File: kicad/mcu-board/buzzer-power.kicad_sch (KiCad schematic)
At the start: 2 parts, among them Q1 Q_NPN_CEB

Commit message: chore?: Saving again, might redo pcb
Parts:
- renumbered R8 to R10
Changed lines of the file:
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@@
 		(dnp no)
 		(fields_autoplaced yes)
-		(property "Reference" "R8"
+		(property "Reference" "R10"
 			(at 99.06 62.23 90)
 			(effects
@@
 			(project ""
 				(path "/f6735569-a094-4d1f-804a-28898efbaebf/56e29116-eeed-430d-b848-aa0aa6b02ec3"
-					(reference "R8")
+					(reference "R10")
 					(unit 1)
 				)

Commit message: chore: Fixed led footprint from 0805 to 0603, and edited title for buzzer
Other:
- company: The Retrievers -> The Retrievers | Designed by aids
- title: (none) -> Buzzer Power
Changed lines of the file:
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@@
 	(paper "A4")
 	(title_block
+		(title "Buzzer Power")
 		(date "2025-12-10")
 		(rev "V1")
-		(company "The Retrievers")
+		(company "The Retrievers | Designed by aids")
 	)
 	(text "Buzzer Power"

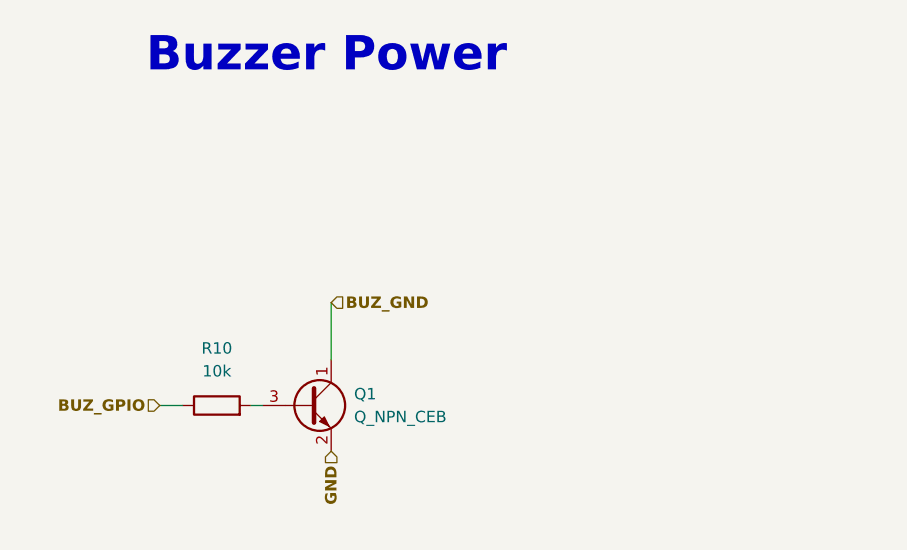
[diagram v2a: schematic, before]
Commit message: feat: finished v2 schematic of mcu-board
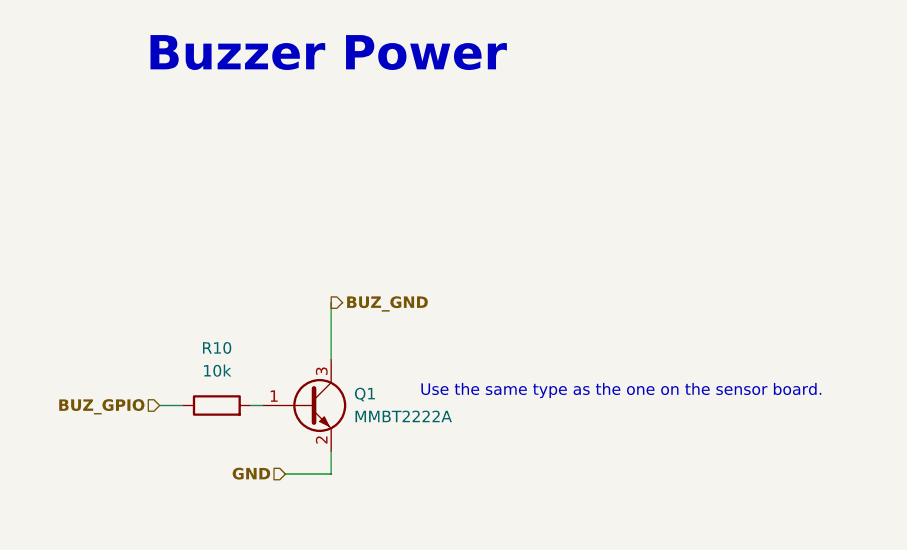
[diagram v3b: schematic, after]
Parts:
- removed Q1: Q_NPN_CEB, Package_TO_SOT_SMD:SOT-23-3, symbol Transistor_BJT:Q_NPN_CEB
- added Q1: MMBT2222A, Package_TO_SOT_SMD:SOT-23, symbol Transistor_BJT:MMBT2222A
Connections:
- net BUZ_GND: now also Q1.3 (C)
- net GND: now also Q1.2 (E)
- net at R10.2: now also Q1.1 (B)
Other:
- note added: "Use the same type as the one on the sensor board."
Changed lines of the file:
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@@
 	(title_block
 		(title "Buzzer Power")
-		(date "2025-12-10")
-		(rev "V1")
+		(date "2026-01-27")
+		(rev "V2")
 		(company "The Retrievers | Designed by aids")
 	)
+	(text "Use the same type as the one on the sensor board."
+		(exclude_from_sim no)
+		(at 144.018 67.056 0)
+		(effects
+			(font
+				(size 1.27 1.27)
+			)
+		)
+	)
 	(text "Buzzer Power"
 		(exclude_from_sim no)
@@
 	(wire
 		(pts
+			(xy 106.68 76.2) (xy 111.76 76.2)
+		)
+		(stroke
+			(width 0)
+			(type default)
+		)
+	)
+	(wire
+		(pts
 			(xy 102.87 68.58) (xy 104.14 68.58)
+		)
+		(stroke
+			(width 0)
+			(type default)
+		)
+	)
+	(wire
+		(pts
+			(xy 111.76 76.2) (xy 111.76 73.66)
 		)
 		(stroke
@@
 	)
 	(hierarchical_label "BUZ_GND"
-		(shape input)
+		(shape output)
 		(at 111.76 57.15 0)
 		(effects
@@
 	(hierarchical_label "GND"
 		(shape input)
-		(at 111.76 73.66 270)
+		(at 106.68 76.2 180)
 		(effects
 			(font
@@
 	)
 	(symbol
-		(lib_id "Transistor_BJT:Q_NPN_CEB")
+		(lib_id "Transistor_BJT:MMBT2222A")
 		(at 109.22 68.58 0)
 		(unit 1)
@@
 			)
 		)
-		(property "Value" "Q_NPN_CEB"
+		(property "Value" "MMBT2222A"
 			(at 114.3 69.8499 0)
 			(effects
@@
 			)
 		)
-		(property "Footprint" "Package_TO_SOT_SMD:SOT-23-3"
-			(at 114.3 66.04 0)
-			(effects
-				(font
-					(size 1.27 1.27)
-				)
-				(hide yes)
-			)
-		)
-		(property "Datasheet" "~"
+		(property "Footprint" "Package_TO_SOT_SMD:SOT-23"
+			(at 114.3 70.485 0)
+			(effects
+				(font
+					(size 1.27 1.27)
+					(italic yes)
+				)
+				(justify left)
+				(hide yes)
+			)
+		)
+		(property "Datasheet" "https://assets.nexperia.com/documents/data-sheet/MMBT2222A.pdf"
 			(at 109.22 68.58 0)
 			(effects
@@
 					(size 1.27 1.27)
 				)
-				(hide yes)
-			)
-		)
-		(property "Description" "NPN transistor, collector/emitter/base"
+				(justify left)
+				(hide yes)
+			)
+		)
+		(property "Description" "600mA Ic, 40V Vce, NPN Transistor, SOT-23"
 			(at 109.22 68.58 0)
 			(effects
@@
 			)
 		)
+		(pin "2"
+		)
+		(pin "3"
+		)
 		(pin "1"
 		)
-		(pin "2"
-		)
-		(pin "3"
-		)
 		(instances

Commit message: feat: finished pcb, might add more artwork later?
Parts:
- removed Q1: MMBT2222A, Package_TO_SOT_SMD:SOT-23, symbol Transistor_BJT:MMBT2222A
- added Q1: MMBT619, Package_TO_SOT_SMD:SOT-23, symbol Transistor_BJT:Q_NPN_BEC
- renumbered R10 to R9
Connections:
- net BUZ_GND: now also Q1.3 (C)
- net GND: now also Q1.2 (E)
- net at R9.2: now also Q1.1 (B)
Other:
- note added: "BUZZER_IO38 Power"
- note removed: "Buzzer Power"
- note removed: "Use the same type as the one on the sensor board."
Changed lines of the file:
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@@
 		(rev "V2")
 		(company "The Retrievers | Designed by aids")
-	)
-	(text "Use the same type as the one on the sensor board."
-		(exclude_from_sim no)
-		(at 144.018 67.056 0)
-		(effects
-			(font
-				(size 1.27 1.27)
-			)
-		)
-	)
-	(text "Buzzer Power"
+		(comment 1 "Balls")
+	)
+	(text "BUZZER_IO38 Power"
 		(exclude_from_sim no)
 		(at 111.252 29.718 0)
@@
 		)
 	)
-	(hierarchical_label "GND"
-		(shape input)
-		(at 106.68 76.2 180)
-		(effects
-			(font
-				(size 1.27 1.27)
-				(thickness 0.254)
-				(bold yes)
-			)
-			(justify right)
-		)
-	)
 	(symbol
 		(lib_id "Device:R")
@@
 		(dnp no)
 		(fields_autoplaced yes)
-		(property "Reference" "R10"
+		(property "Reference" "R9"
 			(at 99.06 62.23 90)
 			(effects
@@
 		)
 		(instances
-			(project ""
+			(project "mcu-board"
 				(path "/f6735569-a094-4d1f-804a-28898efbaebf/56e29116-eeed-430d-b848-aa0aa6b02ec3"
-					(reference "R10")
+					(reference "R9")
 					(unit 1)
 				)
@@
 	)
 	(symbol
-		(lib_id "Transistor_BJT:MMBT2222A")
+		(lib_id "Transistor_BJT:Q_NPN_BEC")
 		(at 109.22 68.58 0)
 		(unit 1)
@@
 			)
 		)
-		(property "Value" "MMBT2222A"
+		(property "Value" "MMBT619"
 			(at 114.3 69.8499 0)
 			(effects
@@
 		)
 		(property "Footprint" "Package_TO_SOT_SMD:SOT-23"
-			(at 114.3 70.485 0)
-			(effects
-				(font
-					(size 1.27 1.27)
-					(italic yes)
-				)
-				(justify left)
-				(hide yes)
-			)
-		)
-		(property "Datasheet" "https://assets.nexperia.com/documents/data-sheet/MMBT2222A.pdf"
+			(at 114.3 66.04 0)
+			(effects
+				(font
+					(size 1.27 1.27)
+				)
+				(hide yes)
+			)
+		)
+		(property "Datasheet" "~"
 			(at 109.22 68.58 0)
 			(effects
@@
 					(size 1.27 1.27)
 				)
-				(justify left)
-				(hide yes)
-			)
-		)
-		(property "Description" "600mA Ic, 40V Vce, NPN Transistor, SOT-23"
+				(hide yes)
+			)
+		)
+		(property "Description" "NPN transistor, base/emitter/collector"
 			(at 109.22 68.58 0)
 			(effects
@@
 			)
 		)
+		(pin "3"
+		)
+		(pin "1"
+		)
 		(pin "2"
 		)
-		(pin "3"
-		)
-		(pin "1"
-		)
 		(instances
-			(project ""
+			(project "mcu-board"
 				(path "/f6735569-a094-4d1f-804a-28898efbaebf/56e29116-eeed-430d-b848-aa0aa6b02ec3"
 					(reference "Q1")
 					(unit 1)
 				)
+			)
+		)
+	)
+	(symbol
+		(lib_id "power:GND")
+		(at 106.68 76.2 0)
+		(unit 1)
+		(exclude_from_sim no)
+		(in_bom yes)
+		(on_board yes)
+		(dnp no)
+		(fields_autoplaced yes)
+		(property "Reference" "#PWR047"
+			(at 106.68 82.55 0)
+			(effects
+				(font
+					(size 1.27 1.27)
+				)
+				(hide yes)
+			)
+		)
+		(property "Value" "GND"
+			(at 106.68 81.28 0)
+			(effects
+				(font
+					(size 1.27 1.27)
+				)
+			)
+		)
+		(property "Footprint" ""
+			(at 106.68 76.2 0)
+			(effects
+				(font
+					(size 1.27 1.27)
+				)
+				(hide yes)
+			)
+		)
+		(property "Datasheet" ""
+			(at 106.68 76.2 0)
+			(effects
+				(font
+					(size 1.27 1.27)
+				)
+				(hide yes)
+			)
+		)
+		(property "Description" "Power symbol creates a global label with name \"GND\" , ground"
+			(at 106.68 76.2 0)
+			(effects
+				(font
+					(size 1.27 1.27)
+				)
+				(hide yes)
+			)
+		)
+		(pin "1"
+		)
+		(instances
+			(project "mcu-board"
+				(path "/f6735569-a094-4d1f-804a-28898efbaebf/56e29116-eeed-430d-b848-aa0aa6b02ec3"
+					(reference "#PWR047")
+					(unit 1)
+				)
